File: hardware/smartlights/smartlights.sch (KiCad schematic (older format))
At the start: 23 parts, among them J1 Conn_01x02_MountingPin, J10 Conn_Coaxial_Power, J11 Raspberry_Pi_2_3, J2 Conn_01x04, J3 Conn_01x02_MountingPin, J4 Conn_01x02_MountingPin, J5 Conn_01x02_MountingPin, J6 Conn_01x02_MountingPin, J7 Conn_01x02_MountingPin, J8 Conn_01x02_MountingPin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

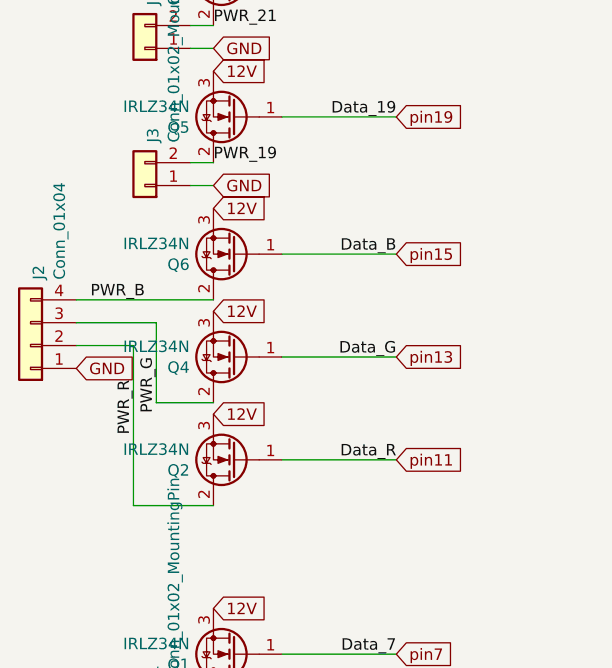
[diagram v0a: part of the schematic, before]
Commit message: Fix wrong voltage on transistors
Also, the RGB Strip has shared 12V, not GND.
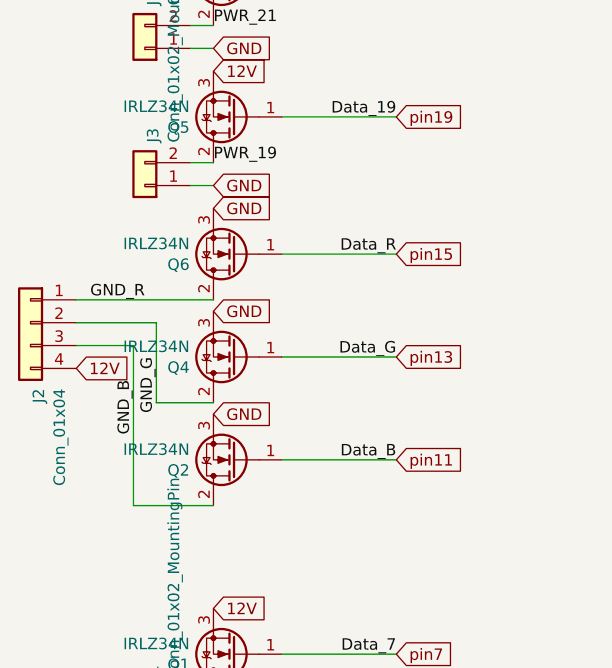
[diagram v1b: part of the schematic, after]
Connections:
- net +12V: now also J2.4 (Pin_4); no longer Q2.3 (S), Q4.3 (S), Q6.3 (S)
- net GND: now also Q2.3 (S), Q4.3 (S), Q6.3 (S); no longer J2.1 (Pin_1)
- net PWR_B renamed GND_R
- net GND_R: now also J2.1 (Pin_1); no longer J2.4 (Pin_4)
- net PWR_G renamed GND_B
- net GND_B: now also Q2.2 (D); no longer Q4.2 (D)
- net PWR_R renamed GND_G
- net GND_G: now also Q4.2 (D); no longer Q2.2 (D)
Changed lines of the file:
@@
-	-1   0    0    1
-$EndComp
-$Comp
-L Connector_Generic:Conn_01x04 J2
-U 1 1 5E66A677
-P 900 4250
-F 0 "J2" V 864 3962 50  0000 R CNN
-F 1 "Conn_01x04" V 773 3962 50  0000 R CNN
-F 2 "Connector_PinHeader_2.54mm:PinHeader_1x04_P2.54mm_Vertical" H 900 4250 50  0001 C CNN
-F 3 "~" H 900 4250 50  0001 C CNN
-	1    900  4250
 	-1   0    0    1
 $EndComp
@@
 Text GLabel 1700 2950 2    50   Input ~ 0
 GND
-Text GLabel 1100 4350 2    50   Input ~ 0
-GND
 Text GLabel 1700 3550 2    50   Input ~ 0
 GND
@@
 Text GLabel 1700 5400 2    50   Input ~ 0
 12V
-Text GLabel 1700 3650 2    50   Input ~ 0
-12V
 Text GLabel 1700 4100 2    50   Input ~ 0
-12V
-Text GLabel 1700 4550 2    50   Input ~ 0
-12V
+GND
 Text GLabel 1700 2450 2    50   Input ~ 0
 12V
@@
 	1450 4500 1700 4500
 Text Label 1350 4400 3    50   ~ 0
-PWR_R
+GND_B
 Text Label 1450 4300 3    50   ~ 0
-PWR_G
+GND_G
 Text Label 1400 4050 2    50   ~ 0
-PWR_B
+GND_R
 Wire Wire Line
 	1600 5800 1700 5800
@@
 	1600 2850 1700 2850
 Text Label 2500 3850 2    50   ~ 0
-Data_B
+Data_R
 Text Label 2500 4300 2    50   ~ 0
 Data_G
 Text Label 2500 4750 2    50   ~ 0
-Data_R
+Data_B
 Text Label 2500 3250 2    50   ~ 0
 Data_19
@@
 	4300 5500 4300 5400
 Connection ~ 4600 5500
+Text GLabel 1700 3650 2    50   Input ~ 0
+GND
+Text GLabel 1700 4550 2    50   Input ~ 0
+GND
+$Comp
+L Connector_Generic:Conn_01x04 J2
+U 1 1 5E66A677
+P 900 4150
+F 0 "J2" V 864 3862 50  0000 R CNN
+F 1 "Conn_01x04" V 773 3862 50  0000 R CNN
+F 2 "Connector_PinHeader_2.54mm:PinHeader_1x04_P2.54mm_Vertical" H 900 4150 50  0001 C CNN
+F 3 "~" H 900 4150 50  0001 C CNN
+	1    900  4150
+	-1   0    0    -1
+$EndComp
+Text GLabel 1100 4350 2    50   Input ~ 0
+12V
 $EndSCHEMATC
